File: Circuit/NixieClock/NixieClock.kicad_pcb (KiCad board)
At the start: 2 copper layers, 2 parts, among them U1 74141N

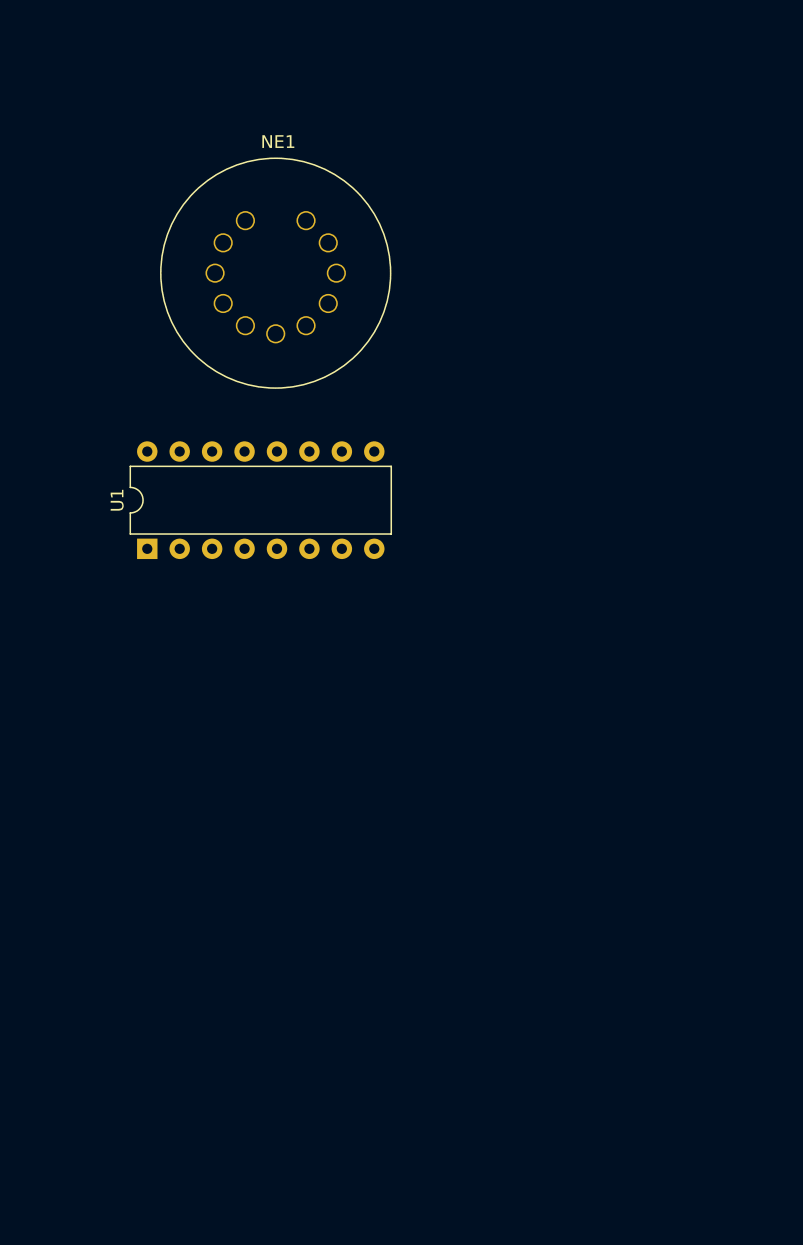
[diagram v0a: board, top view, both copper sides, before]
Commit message: Migrate to Kicad6
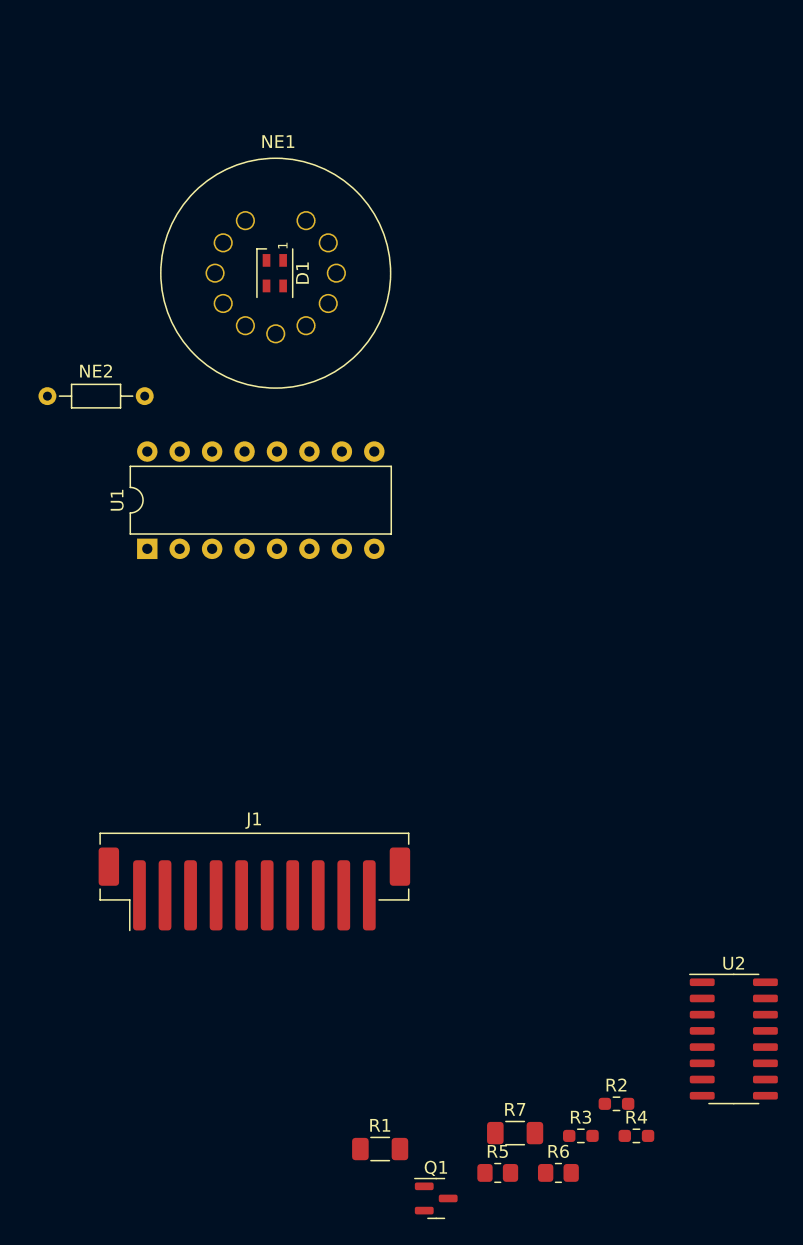
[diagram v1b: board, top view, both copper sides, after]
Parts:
- added D1: LED_RGBA, LED_SMD:LED_SK6805_PLCC4_2.4x2.7mm_P1.3mm, F.Cu at (39.2, 39.4)
- added J1: Conn_01x10, Connector_JST:JST_PH_B10B-PH-SM4-TB_1x10-1MP_P2.00mm_Vertical, F.Cu at (37.6, 87.6)
- added NE2: Lamp_Neon, Resistor_THT:R_Axial_DIN0204_L3.6mm_D1.6mm_P7.62mm_Horizontal, F.Cu at (21.4, 49.0)
- added Q1: MMBTA42, Package_TO_SOT_SMD:SOT-23, F.Cu at (51.8, 111.8)
- added R1: 8k, Resistor_SMD:R_1206_3216Metric_Pad1.30x1.75mm_HandSolder, F.Cu at (47.5, 108.0)
- added R2: 150, Resistor_SMD:R_0603_1608Metric_Pad0.98x0.95mm_HandSolder, F.Cu at (66.0, 104.4)
- added R3: 100, Resistor_SMD:R_0603_1608Metric_Pad0.98x0.95mm_HandSolder, F.Cu at (63.2, 106.9)
- added R4: 100, Resistor_SMD:R_0603_1608Metric_Pad0.98x0.95mm_HandSolder, F.Cu at (67.5, 106.9)
- added R5: 100k, Resistor_SMD:R_0805_2012Metric_Pad1.20x1.40mm_HandSolder, F.Cu at (56.7, 109.8)
- added R6: 1M, Resistor_SMD:R_0805_2012Metric_Pad1.20x1.40mm_HandSolder, F.Cu at (61.4, 109.8)
- added R7: 150k, Resistor_SMD:R_1206_3216Metric_Pad1.30x1.75mm_HandSolder, F.Cu at (58.0, 106.7)
- added U2: 74AHC595, Package_SO:SOIC-16_3.9x9.9mm_P1.27mm, F.Cu at (75.2, 99.3)
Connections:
- U1 pad 12: Net-(U1-Pad12) -> GND
- U1 pad 5: Net-(U1-Pad5) -> +5V
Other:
- net class Default removed

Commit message: Set Conn Pin 4 as GND, Rule, and Board Shape
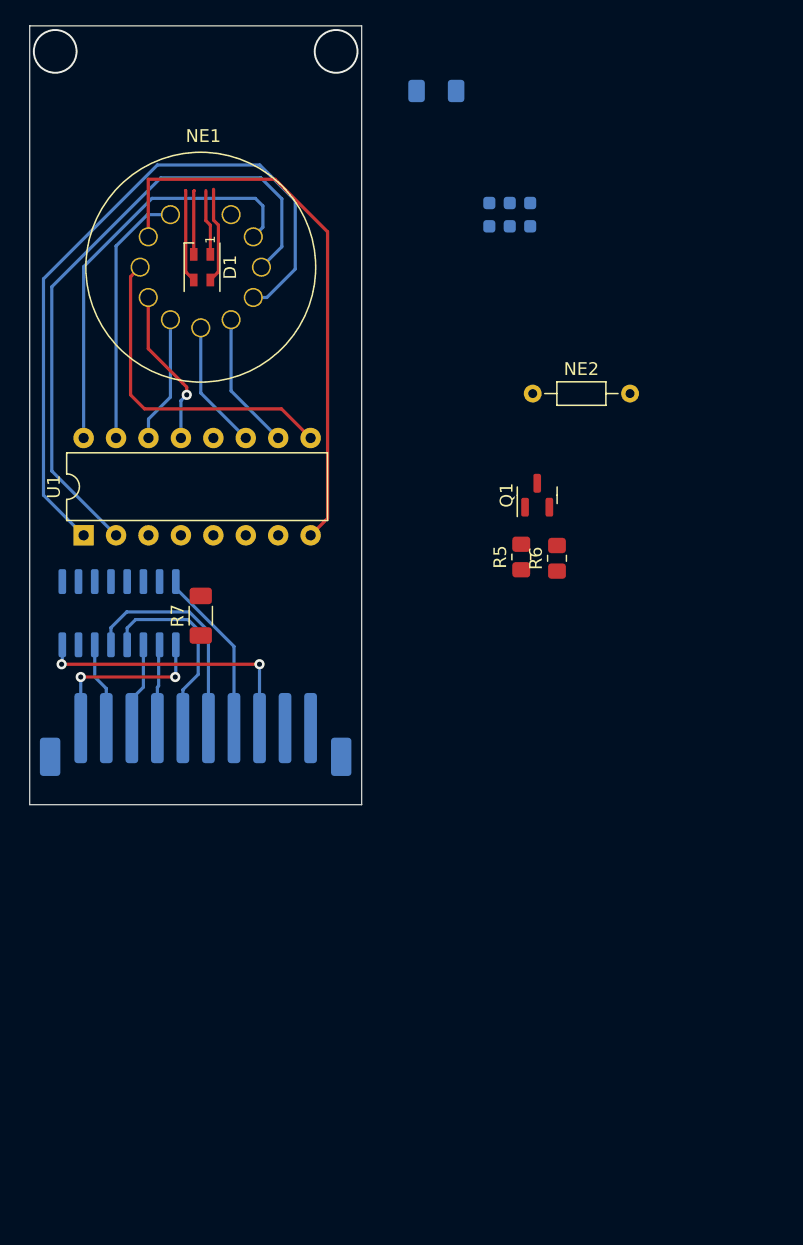
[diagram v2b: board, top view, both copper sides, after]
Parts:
- J1, R1, R2, R3, R4, U2: moved to B.Cu
- moved R1 83.0 mm to (51.9, 25.1), turned to 180 degrees
- moved R4 73.1 mm to (56.0, 34.8), turned to -90 degrees
- moved R3 72.3 mm to (59.2, 34.8), turned to -90 degrees
- moved R2 70.1 mm to (57.6, 34.8), turned to -90 degrees
- moved U2 58.6 mm to (27.0, 66.0), turned to -90 degrees
- moved Q1 55.6 mm to (59.8, 56.8), turned to 90 degrees
- moved R5 48.3 mm to (58.5, 61.6), turned to 90 degrees
- moved R6 48.1 mm to (61.3, 61.7), turned to 90 degrees
- moved R7 47.4 mm to (33.4, 66.2), turned to 90 degrees
- moved NE2 38.0 mm to (59.4, 48.8)
- moved J1 12.9 mm to (33.0, 75.5)
- moved NE1 5.89 mm to (33.5, 38.9)
- moved D1 5.72 mm to (33.5, 38.9)
- moved U1 5.10 mm to (24.2, 59.9)
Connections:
- J1 pad 7: unconnected-(J1-Pad7) -> GND
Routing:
- net Net-(NE1-Pad8): track 0.00 -> 55.5 mm
- net Net-(NE1-Pad9): track 0.00 -> 49.8 mm
- net Net-(NE1-Pad2): track 0.00 -> 44.6 mm
- net Net-(NE1-Pad10): track 0.00 -> 32.6 mm
- net +5V: track 0.00 -> 29.6 mm, vias 0 -> 2
- net Net-(NE1-Pad3): track 0.00 -> 25.8 mm
- net Net-(NE1-Pad1): track 0.00 -> 20.3 mm
- net /EN: track 0.00 -> 17.7 mm
- net /LATCH: track 0.00 -> 15.7 mm
- net /SER_OUT: track 0.00 -> 13.9 mm, vias 0 -> 2
- net GND: track 0.00 -> 13.4 mm
- net Net-(NE1-Pad4): track 0.00 -> 12.4 mm, vias 0 -> 1
- net Net-(NE1-Pad7): track 0.00 -> 10.8 mm
- net Net-(NE1-Pad6): track 0.00 -> 10.1 mm
- net Net-(NE1-Pad5): track 0.00 -> 9.98 mm
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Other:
- board outline added: 26 x 61 mm

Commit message: Complete Route NIXIE tube to Driver
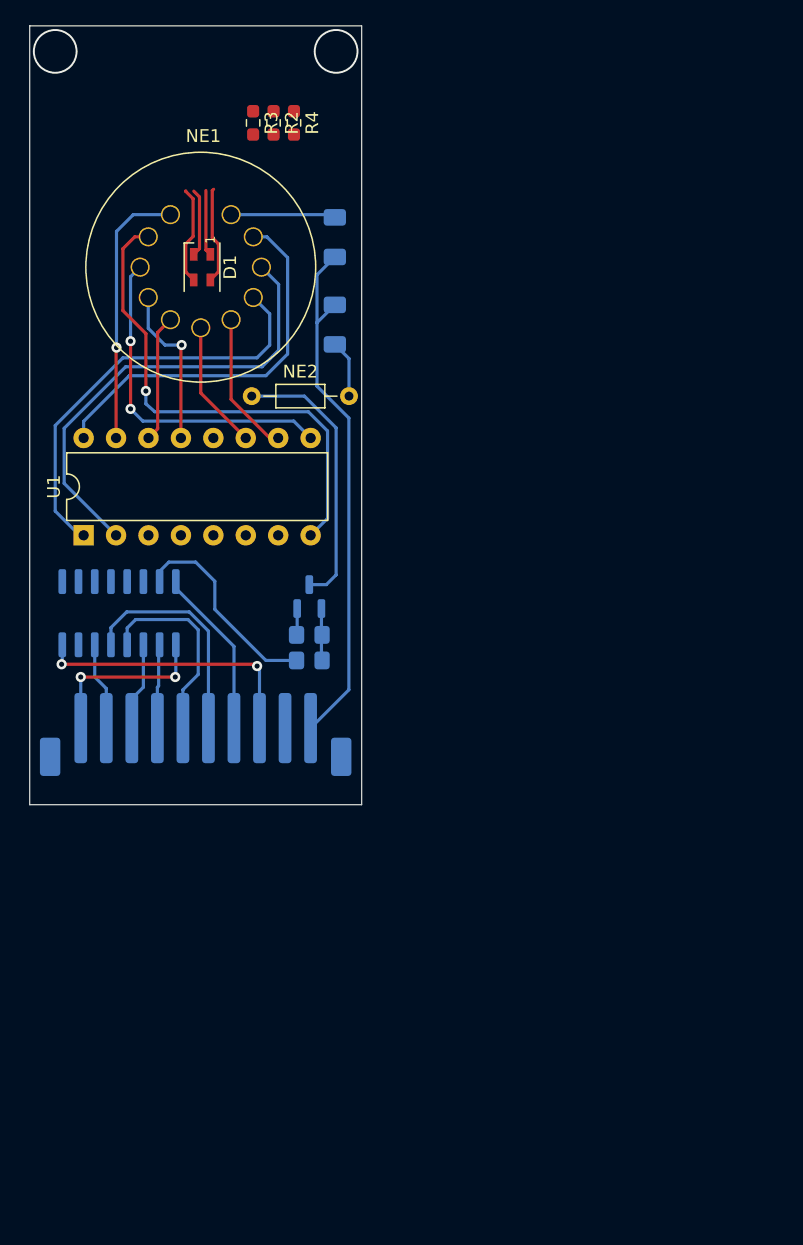
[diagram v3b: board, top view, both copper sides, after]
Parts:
- Q1, R5, R6, R7: moved to B.Cu
- R2, R3, R4: moved to F.Cu
- moved R7 25.1 mm to (43.9, 43.4), turned to -90 degrees
- moved R3 22.9 mm to (37.5, 27.6)
- moved NE2 22.0 mm to (37.4, 49.0)
- moved R6 20.3 mm to (41.9, 67.7), turned to 0 degrees
- moved R2 19.8 mm to (39.1, 27.6)
- moved Q1 19.5 mm to (41.9, 64.7)
- moved R5 18.5 mm to (41.9, 69.7), turned to 0 degrees
- moved R4 16.9 mm to (40.7, 27.6)
- moved R1 13.9 mm to (43.9, 36.5), turned to 90 degrees
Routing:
- net /HV_DC: track 0.00 -> 41.7 mm
- net Net-(NE1-Pad8): track 55.5 -> 33.4 mm
- net Net-(NE2-Pad1): track 0.00 -> 21.6 mm
- net Net-(R5-Pad1): track 0.00 -> 16.3 mm
- net Net-(NE1-Pad9): track 49.8 -> 36.5 mm
- net Net-(NE1-Pad11): track 0.00 -> 8.08 mm
- net Net-(NE1-Pad2): track 44.6 -> 39.1 mm, vias 0 -> 1
- net Net-(NE2-Pad2): track 0.00 -> 4.51 mm
- net Net-(Q1-Pad1): track 0.00 -> 4.08 mm
- net Net-(NE1-Pad10): track 32.6 -> 30.4 mm
- net GND: track 13.4 -> 15.4 mm
- net Net-(NE1-Pad3): track 25.8 -> 26.8 mm, vias 0 -> 2
- net Net-(NE1-Pad1): track 20.3 -> 21.0 mm, vias 0 -> 1

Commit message: Complete Route
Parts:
- moved R2 41.6 mm to (23.0, 66.0)
- moved R4 41.0 mm to (26.2, 66.0)
- moved R3 40.5 mm to (24.6, 66.0)
- moved Q1 3.07 mm to (39.0, 63.7)
- moved R5 3.07 mm to (39.0, 68.7)
- moved R6 3.07 mm to (39.0, 66.7)
- moved R1 2.51 mm to (42.2, 38.4)
- moved R7 1.70 mm to (42.2, 43.4)
- moved NE2 0.50 mm to (37.0, 48.7)
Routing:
- net +5V: track 29.5 -> 89.5 mm, vias 2 -> 3
- net Net-(D1-Pad1): track 5.14 -> 46.4 mm
- net Net-(D1-Pad2): track 5.32 -> 46.1 mm
- net Net-(D1-Pad3): track 7.72 -> 47.2 mm
- net Net-(R2-Pad2): track 0.00 -> 22.4 mm, vias 0 -> 1
- net Net-(U1-Pad7): track 0.00 -> 18.4 mm, vias 0 -> 1
- net Net-(R3-Pad2): track 0.00 -> 17.5 mm, vias 0 -> 1
- net Net-(U1-Pad6): track 0.00 -> 16.9 mm, vias 0 -> 1
- net Net-(U1-Pad3): track 0.00 -> 15.9 mm
- net Net-(R4-Pad2): track 0.00 -> 12.2 mm, vias 0 -> 1
- net Net-(U1-Pad4): track 0.00 -> 8.47 mm
- net Net-(NE1-Pad8): track 33.4 -> 39.5 mm
- net Net-(NE1-Pad9): track 36.5 -> 40.2 mm
- net Net-(R5-Pad1): track 16.3 -> 13.2 mm
- net /HV_DC: track 41.7 -> 38.6 mm
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- added copper zone on B.Cu, net /HV_DC
- added copper zone on B.Cu, net GND
- added copper zone on F.Cu, net GND
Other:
- board size 26 x 61 mm -> 26 x 52.1 mm

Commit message: Generate Gerber File
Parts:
- added REF**: KiCad-Logo_5mm_SilkScreen, Symbol:KiCad-Logo_5mm_SilkScreen, F.Cu at (38.8, 78.0)
- added REF**: Symbol_HighVoltage_Type2_SilkScreen_VerySmall, NixieClock:Symbol_HighVoltage_Type2_SilkScreen_VerySmall, B.Cu at (25.8, 46.2)
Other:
- board size 26 x 52.1 mm -> 26 x 52 mm
- board text added: "NIXIE TUBE For IN-8 and NE-8 HV_DC: 170V Vcc: 5V"
